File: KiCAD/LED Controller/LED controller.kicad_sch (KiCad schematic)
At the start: 3 parts, among them J1 Conn_01x24_Female, J2 Conn_01x24_Female, U1 Teensy4.1

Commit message: Working draft of driver circuit
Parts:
- added J3: 4x RJ45, Custom Footprints:RJ45_x4-RJSSE-5380-04, symbol Custom:4x_RJ45
- added PS1, PS2: 15V DC-DC, Custom Footprints:SRS-1215-2, symbol Custom:DC-DC_15V
- added RN1, RN3: 3600, Resistor_SMD:R_Array_Convex_4x0603, symbol Device:R_Pack04
- added RN2: 390, Resistor_SMD:R_Array_Convex_4x0603, symbol Device:R_Pack04
- added RV1, RV2, RV3: 10k, Custom Footprints:P160KN2-4QC20B10K, symbol Device:R_Potentiometer
- added SW1, SW2, SW3: ELUMOASAQ2C22, Custom Footprints:ELUMOASAQ2C22_CNK, symbol Custom:ELUMOASAQ2C22
- added U2, U3, U4: SN75374D, Custom Footprints:D16-4x gate driver, symbol Custom:SN75374D
- added U5: SN74LV4053ADR, Custom Footprints:SN74LV4053ADR, symbol Custom:SN74LV4053ADR
- added U6: DAC084S085CIMMX/NOPB, Custom Footprints:DAC084S085CIMMXNOPB, symbol Custom:DAC084S085CIMMX_NOPB
- added U7: NXB0104PWJ, Custom Footprints:TSSOP14_NXB0104_NEX, symbol Custom:NXB0104PWJ
- J1: footprint Custom Footprints:Ref_only -> (none); Part (none) -> SSM-124-L-SV-LC; Part # SSM-124-L-SV-LC -> (none)
- J2: Part (none) -> SSM-124-L-SV-LC; Part # SSM-124-L-SV-LC -> (none)
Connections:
- net PWM3 is gone; now on net SW3 red: J1.~, U1.4 (2_OUT2)
- net 3v3: now also PS1.11, PS1.6 (-Vout), RN1.8 (R1.2), RN3.1 (R1.1), RN3.2 (R2.1), RN3.3 (R3.1), RN3.4 (R4.1), RV1.1, RV2.1, RV3.1, U2.12 (2E1), U2.13 (2E2), U2.4 (1E1), U2.5 (1E2), U3.12 (2E1), U3.13 (2E2), U3.4 (1E1), U3.5 (1E2), U4.12 (2E1), U4.13 (2E2), U4.4 (1E1), U4.5 (1E2), U5.16 (VCC), U6.1 (VA), U6.7 (VREFIN), U7.1 (VCC(A))
- net 5V: now also PS2.10, PS2.7 (+Vout), RN1.2 (R2.1), RN1.3 (R3.1), RN1.4 (R4.1), U2.16 (VCC1), U3.16 (VCC1), U4.16 (VCC1), U7.14 (VCC(B))
- net CS: now also U6.9 (~SYNC)
- net GND: now also J3.10, J3.18, J3.2, J3.26, J3.28, J3.30, J3.SH, J3.SH, J3.SH, J3.SH, PS1.8 (-Vin), PS1.9, PS2.11, PS2.6 (-Vout), PS2.8 (-Vin), PS2.9, RN1.5 (R4.2), RN1.6 (R3.2), RN1.7 (R2.2), RV1.3, RV2.3, RV3.3, SW1.2, SW2.2, SW3.2, U2.8 (GND), U3.8 (GND), U4.8 (GND), U5.12 (1Y0), U5.2 (2Y0), U5.5 (3Y0), U5.7 (GND), U5.8 (GND), U6.6 (GND), U7.10 (B4), U7.5 (A4), U7.7 (GND)
- net MOSI: now also U6.8 (DIN)
- net SCK: now also U6.10 (SCLK)
- net SW1: now also SW1.3
- net SW1 green: now also U1.9 (7_RX2_OUT1A), SW1.1; no longer U1.7 (5_IN2)
- net SW1 red: now also U1.10 (8_TX2_IN1), RN2.4 (R4.1); no longer U1.6 (4_BCLK2)
- net SW2: now also SW2.3
- net SW2 green: now also U1.11 (9_OUT1C), SW2.1; no longer U1.9 (7_RX2_OUT1A)
- net SW2 red: now also RN2.3 (R3.1)
- net SW3: now also SW3.3
- net SW3 green: now also U1.5 (3_LRCLK2), SW3.1; no longer U1.11 (9_OUT1C)
- net SW3 red: now also RN2.2 (R2.1); no longer U1.10 (8_TX2_IN1)
- net Temp1: now also J3.6, RN3.5 (R4.2)
- net Temp2: now also J3.14, RN3.6 (R3.2)
- net Temp3: now also J3.22, RN3.7 (R2.2)
- net Ch1 renamed Pot3
- net Pot3: now also RV3.2
- net Ch10 renamed Ch2b
- net Ch2b: now also U3.6 (2A)
- net Ch11 renamed Ch2c
- net Ch2c: now also U3.11 (3A)
- net Ch12 renamed Ch2d
- net Ch2d: now also U3.14 (4A)
- net Ch13 renamed Ch3a
- net Ch3a: now also U4.3 (1A)
- net Ch14 renamed Ch3b
- net Ch3b: now also U4.6 (2A)
- net Ch15 renamed Ch3c
- net Ch3c: now also U4.11 (3A)
- net Ch16 renamed Ch3d
- net Ch3d: now also U4.14 (4A)
- net Ch2 renamed Ch1a
- net Ch1a: now also U2.3 (1A)
- net Ch3 renamed Ch1b
- net Ch1b: now also U2.6 (2A)
- net Ch4 renamed Ch1c
- net Ch1c: now also U2.11 (3A)
- net Ch5 renamed Ch1d
- net Ch1d: now also U2.14 (4A)
- net Ch6: no longer names the net of J2.~, U1.35 (13_SCK_LED)
- net Ch7 renamed LED_PWM3
- net LED_PWM3: now also U5.9 (C)
- net Ch8: no longer names the net of J2.~, U1.33 (41_A17)
- net Ch9 renamed Ch2a
- net Ch2a: now also U3.3 (1A)
- net PWM1 renamed Fan_PWM1_low
- net Fan_PWM1_low: now also U7.2 (A1)
- net PWM2 renamed Fan_PWM2_low
- net Fan_PWM2_low: now also U7.3 (A2)
- removed net PWM4: J1.~, U1.5 (3_LRCLK2)
- net Pot renamed Pot2
- net Pot2: now also RV2.2
- net SW4 renamed Ctrl_off
- net Ctrl_off: now also U5.6 (INH)
- net SW4 green renamed LED_PWM2
- net LED_PWM2: now also U5.10 (B)
- net SW4 red renamed LED_PWM1
- net LED_PWM1: now also U5.11 (A)
- net Temp4 renamed Pot1
- net Pot1: now also RV1.2
- new net: RN2.7 (R2.2), SW3.5
- new net: RN2.5 (R4.2), SW1.5
- new net: RN2.6 (R3.2), SW2.5
- new net 1-1: J3.5, U2.2 (1Y)
- new net 1-2: J3.4, U2.7 (2Y)
- new net 1-3: J3.7, U2.10 (3Y)
- new net 1-4: J3.8, U2.15 (4Y)
- new net 12V: J3.1, J3.17, J3.25, J3.27, J3.9, PS1.1 (+Vin), PS1.16, PS2.1 (+Vin), PS2.16
- new net 18V: PS1.10, PS1.7 (+Vout), RN1.1 (R1.1), U2.1 (VCC2), U2.9 (VCC3), U3.1 (VCC2), U3.9 (VCC3), U4.1 (VCC2), U4.9 (VCC3)
- new net 2-1: J3.13, U3.2 (1Y)
- new net 2-2: J3.12, U3.7 (2Y)
- new net 2-3: J3.15, U3.10 (3Y)
- new net 2-4: J3.16, U3.15 (4Y)
- new net 3-1: J3.21, U4.2 (1Y)
- new net 3-2: J3.20, U4.7 (2Y)
- new net 3-3: J3.23, U4.10 (3Y)
- new net 3-4: J3.24, U4.15 (4Y)
- new net Ana1: U5.13 (1Y1), U6.2 (VOUTA)
- new net Ana2: U5.1 (2Y1), U6.3 (VOUTB)
- new net Ana3: U5.3 (3Y1), U6.4 (VOUTC)
- new net Ctrl1: J3.3, U5.14 (1-COM)
- new net Ctrl2: J3.11, U5.15 (2-COM)
- new net Ctrl3: J3.19, U5.4 (3-COM)
- new net Fan_PWM1: J3.29, U7.13 (B1)
- new net Fan_PWM2: J3.31, U7.12 (B2)
- new net Fan_PWM3: J3.32, U7.11 (B3)
- new net Fan_PWM3_low: J1.~, U1.6 (4_BCLK2), U7.4 (A3)
- new net Fan_enable: J1.~, U1.7 (5_IN2), U7.8 (OE)
- no-connect marks 0 -> 7

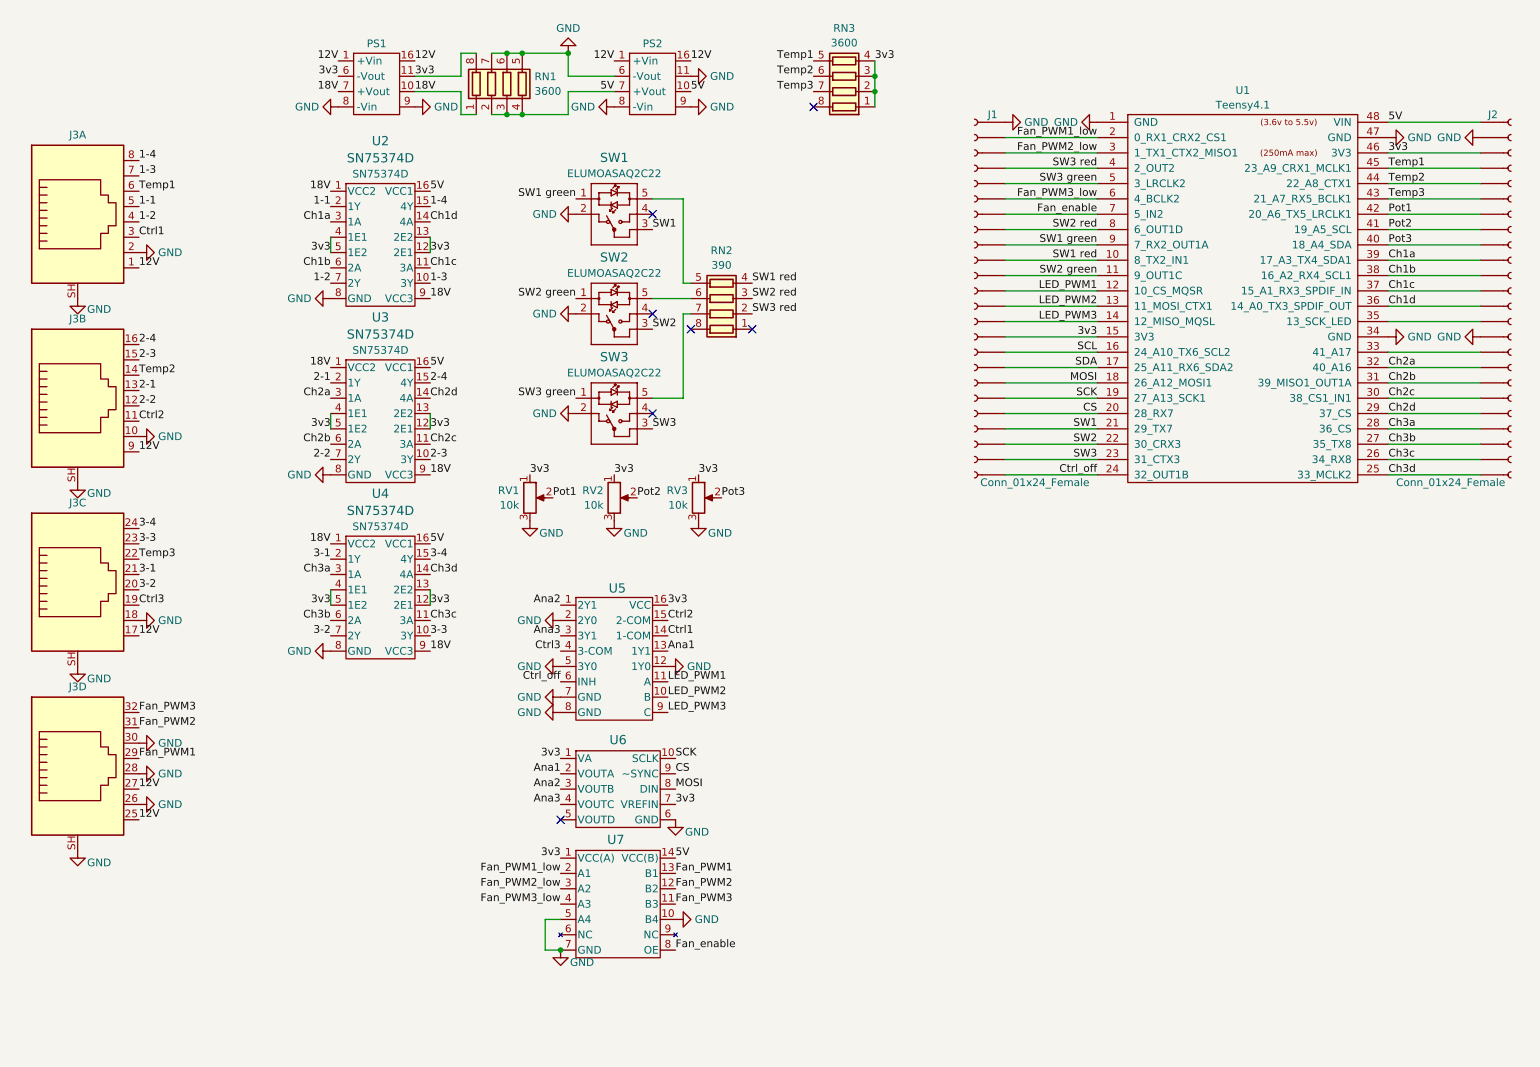
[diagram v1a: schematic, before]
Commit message: bypass caps added
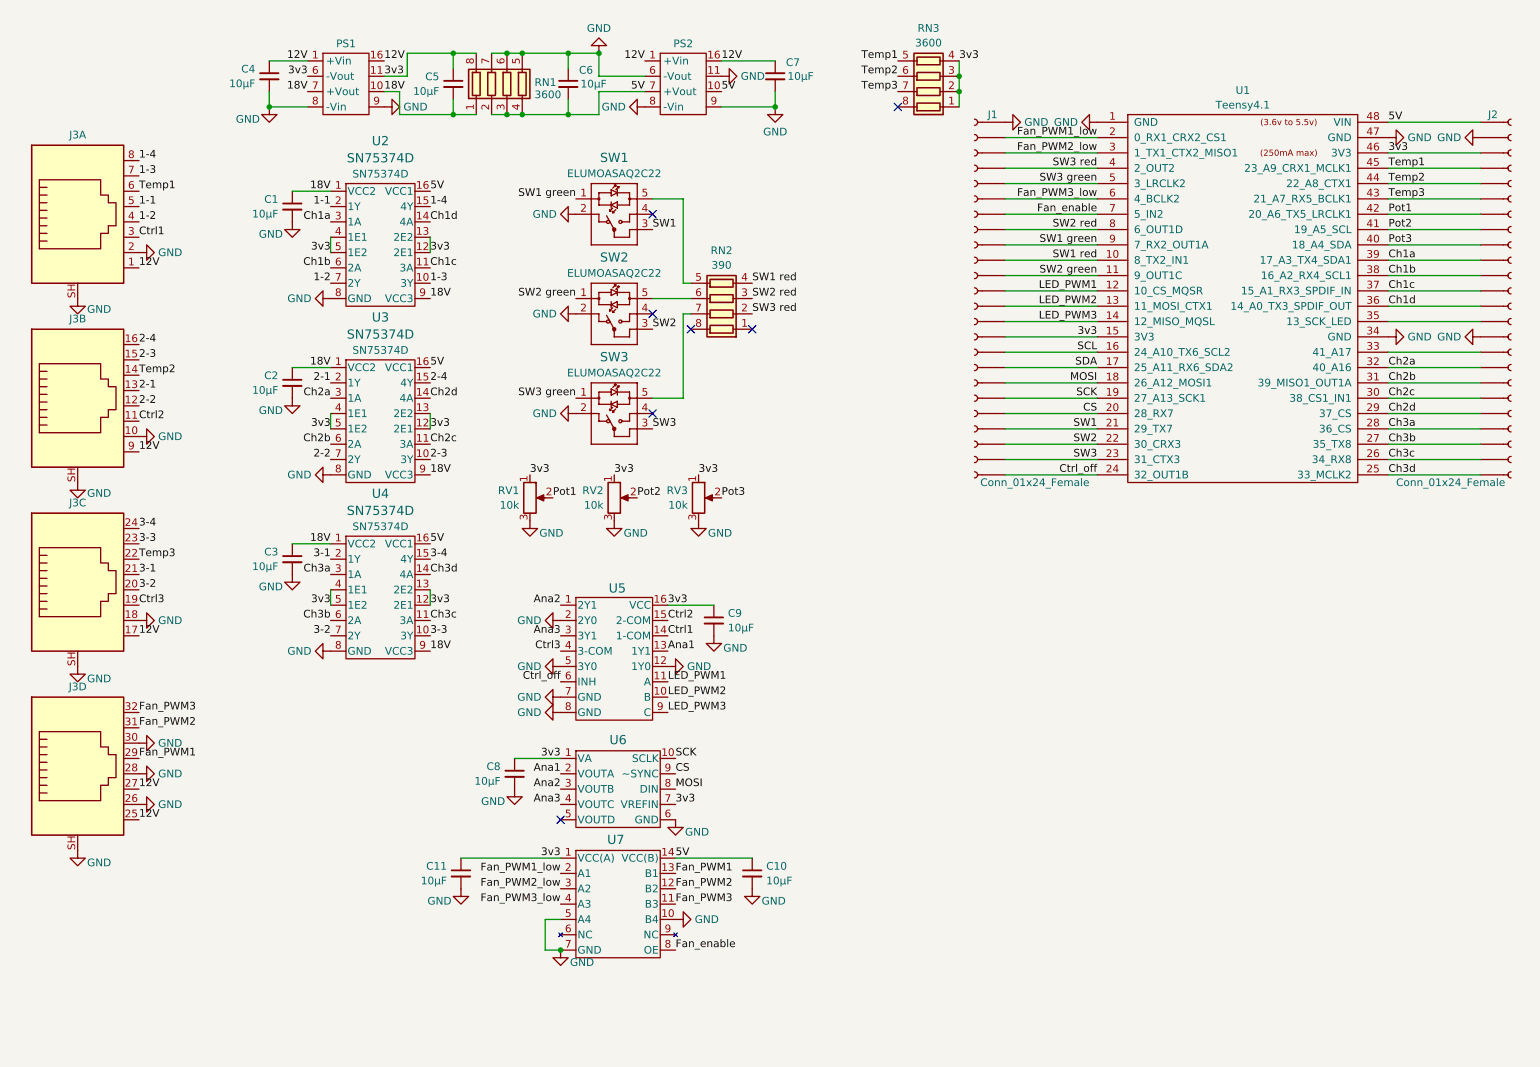
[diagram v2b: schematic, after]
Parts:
- added C1, C10, C11, C2, C3, C4, C5, C6, C7, C8, C9: 10µF, Capacitor_SMD:C_0805_2012Metric, symbol Device:C_Small
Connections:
- net 12V: now also C4.1, C7.1
- net 18V: now also C1.1, C2.1, C3.1, C5.2
- net 3v3: now also C11.1, C5.1, C8.1, C9.1
- net 5V: now also C10.1, C6.2
- net GND: now also C1.2, C10.2, C11.2, C2.2, C3.2, C4.2, C6.1, C7.2, C8.2, C9.2
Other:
- moved on the sheet: PS1, PS2, RN3

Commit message: Partial PCB layout
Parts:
- removed C1: 10µF, Capacitor_SMD:C_0805_2012Metric, symbol Device:C_Small
- added C4: 1µF, Capacitor_SMD:C_0603_1608Metric, symbol Device:C_Small
- added H1, H2, H3, H4: MountingHole, Custom Footprints:1-4_20 standoff, symbol Mechanical:MountingHole
- added J1: Barrel_Jack_Switch, Custom Footprints:DC-jack_54-00165, symbol Connector:Barrel_Jack_Switch
- C1: renamed from C4; value 10µF -> 1µF; footprint Capacitor_SMD:C_0805_2012Metric -> Capacitor_SMD:C_0603_1608Metric; Manufacturer Walsin Technology Corporation -> Samsung Electro-Mechanics; Part 0805X106K250CT -> CL10A105KB8NNNC
- C10, C11, C2, C3, C5, C6, C7, C8, C9: value 10µF -> 1µF; footprint Capacitor_SMD:C_0805_2012Metric -> Capacitor_SMD:C_0603_1608Metric; Manufacturer Walsin Technology Corporation -> Samsung Electro-Mechanics; Part 0805X106K250CT -> CL10A105KB8NNNC
- renumbered J3 to J2, J1 to J3, J2 to J4, RN3 to RN1, RN1 to RN2, RN2 to RN3, U2 to U1, U3 to U2, U1 to U3
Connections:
- net 1-1: now also U1.15 (4Y); no longer U1.2 (1Y)
- net 1-2: now also U1.2 (1Y); no longer U1.7 (2Y)
- net 1-4: now also U1.7 (2Y); no longer U1.15 (4Y)
- net 12V: now also C2.1, J1.1; no longer C7.1
- net 18V: now also C3.2, C5.1, C6.1, C7.1, RN2.8 (R1.2); no longer C2.1, C3.1, C5.2, RN2.1 (R1.1)
- net 2-1: now also U2.15 (4Y); no longer U2.2 (1Y)
- net 2-2: now also U2.2 (1Y); no longer U2.7 (2Y)
- net 2-4: now also U2.7 (2Y); no longer U2.15 (4Y)
- net 3-1: now also U4.15 (4Y); no longer U4.2 (1Y)
- net 3-2: now also U4.2 (1Y); no longer U4.7 (2Y)
- net 3-4: now also U4.7 (2Y); no longer U4.15 (4Y)
- net 3v3: now also C10.1, C3.1, RN2.1 (R1.1); no longer C11.1, C5.1, RN2.8 (R1.2), U1.12 (2E1), U1.13 (2E2), U1.4 (1E1), U1.5 (1E2), U2.12 (2E1), U2.13 (2E2), U2.4 (1E1), U2.5 (1E2), U4.12 (2E1), U4.13 (2E2), U4.4 (1E1), U4.5 (1E2)
- net 5V: now also C11.1, U1.12 (2E1), U1.13 (2E2), U1.4 (1E1), U1.5 (1E2), U2.12 (2E1), U2.13 (2E2), U2.4 (1E1), U2.5 (1E2), U4.12 (2E1), U4.13 (2E2), U4.4 (1E1), U4.5 (1E2), C4.2; no longer C10.1, C6.2
- net Ch1a: now also U1.14 (4A); no longer U1.3 (1A)
- net Ch1b: now also U1.3 (1A); no longer U1.6 (2A)
- net Ch1d: now also U1.6 (2A); no longer U1.14 (4A)
- net Ch2a: now also U2.14 (4A); no longer U2.3 (1A)
- net Ch2b: now also U2.3 (1A); no longer U2.6 (2A)
- net Ch2d: now also U2.6 (2A); no longer U2.14 (4A)
- net Ch3a: now also U4.14 (4A); no longer U4.3 (1A)
- net Ch3b: now also U4.3 (1A); no longer U4.6 (2A)
- net Ch3d: now also U4.6 (2A); no longer U4.14 (4A)
- net GND: now also C5.2, C6.2, C4.1, J1.2, J1.3; no longer C3.2, C6.1
- net Pot1: now also U3.45 (23_A9_CRX1_MCLK1); no longer U3.42 (20_A6_TX5_LRCLK1)
- net Pot2: now also U3.44 (22_A8_CTX1); no longer U3.41 (19_A5_SCL)
- net Pot3: now also U3.43 (21_A7_RX5_BCLK1); no longer U3.40 (18_A4_SDA)
- net Temp1: now also RN1.7 (R2.2), U3.42 (20_A6_TX5_LRCLK1); no longer RN1.5 (R4.2), U3.45 (23_A9_CRX1_MCLK1)
- net Temp2: now also U3.41 (19_A5_SCL); no longer U3.44 (22_A8_CTX1)
- net Temp3: now also RN1.5 (R4.2), U3.40 (18_A4_SDA); no longer RN1.7 (R2.2), U3.43 (21_A7_RX5_BCLK1)
